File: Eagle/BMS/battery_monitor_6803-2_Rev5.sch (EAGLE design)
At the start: 68 parts, among them IC1 MIC2954-03WS, Q1 MOSFET-PCHANNELIRLML2244, Q10 IRF9530, Q2 MOSFET-NCHANNELBSS138, Q3 MOSFET-PCHANNELIRLML2244, Q4 MOSFET-PCHANNELIRLML2244, Q5 MOSFET-PCHANNELIRLML2244, Q6 MOSFET-NCHANNELBSS138, Q7 MOSFET-NCHANNELBSS138, Q8 MOSFET-NCHANNELBSS138, Q9 PMOS_AO4435

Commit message: Added voltage regulator to charging circuit of BMS.
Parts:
- removed A0: (no value), SparkFun:SOLDERJUMPER_2WAYS
- removed U$7: TACTILE-SWITCH-7914G, GeekAmmo:TACTILE-SWITCH-7914G
- removed U$8: ARDUINO_R3_SHIELD, SparkFun-Boards:ARDUINO_R3_SHIELD
- added A4: (no value), SparkFun:SOLDERJUMPER_2WAYS
- added D3: SMD26PL-TP, SparkFun-DiscreteSemi:DIODESOD123
- added X1: W237-07P, con-wago-508:W237-07P
- C1: value 0.1uF -> 1uF; MF AVX CORPORATION -> (none); MPN 0603YG104ZAT2A -> C0603X5R0J105M030BC; OC_NEWARK 01H6821 -> 04X3184; PROD_ID (none) -> CAP-08390; VALUE (none) -> 0.1uF
- C4: value 1uF -> 0.1uF; MF (none) -> AVX CORPORATION; MPN C0603X5R0J105M030BC -> 0603YG104ZAT2A; OC_NEWARK 04X3184 -> 01H6821; PROD_ID CAP-08390 -> (none); VALUE 0.1uF -> (none)
- R11: value 100k -> 4.7k; MF FARNELL -> VISHAY/DALE; MPN MC0063W06035100K -> CRCW06034K70FKEA; OC_NEWARK 39K0075 -> 52K8494
- R12: value 4.7k -> 100k; MF VISHAY/DALE -> FARNELL; MPN CRCW06034K70FKEA -> MC0063W06035100K; OC_NEWARK 52K8494 -> 39K0075
- R15: value 4.7k -> 470; MF VISHAY/DALE -> (none); MPN CRCW06034K70FKEA -> ERJ-P03F4700V; OC_NEWARK 52K8494 -> 05X8640; PROD_ID (none) -> RES-07851
- R17: value 470 -> 4.7k; MF (none) -> VISHAY/DALE; MPN ERJ-P03F4700V -> CRCW06034K70FKEA; OC_NEWARK 05X8640 -> 52K8494; PROD_ID RES-07851 -> (none)
- R18: value 470 -> 4.7k; MF (none) -> VISHAY/DALE; MPN ERJ-P03F4700V -> CRCW06034K70FKEA; OC_NEWARK 05X8640 -> 52K8494
- R20: value 4.7k -> 470; MF VISHAY/DALE -> (none); MPN CRCW06034K70FKEA -> ERJ-P03F4700V; OC_NEWARK 52K8494 -> 05X8640
- R21: value 4.7k -> 1Meg; MF VISHAY/DALE -> (none); MPN CRCW06034K70FKEA -> ERJ-3EKF1004V; OC_NEWARK 52K8494 -> 64R5311
- R24: value 1Meg -> 4.7k; MF (none) -> VISHAY/DALE; MPN ERJ-3EKF1004V -> CRCW06034K70FKEA; OC_NEWARK 64R5311 -> 52K8494
- R3: value 3.3k -> 100; MF VISHAY/DALE -> (none); MPN CRCW06033K00FKEA -> ERJ-1GNF1000C; OC_NEWARK 52K8368 -> 05X8794
- R4: value 100 -> 3.3k; MF (none) -> VISHAY/DALE; MPN ERJ-1GNF1000C -> CRCW06033K00FKEA; OC_NEWARK 05X8794 -> 52K8368
- U$3: value RESISTOR-POWER-3W -> TACTILE-SWITCH-7914G; device isaac1:RESISTOR-POWER-3W -> GeekAmmo:TACTILE-SWITCH-7914G; MF (none) -> BOURNS, INC.; MPN ERG-3SJ200 -> 7914G-1-000E; OC_NEWARK 52W7905 -> 05B2757
- U$4: value SCREW_TERMINAL_4 -> RESISTOR-POWER-3W; device isaac1:SCREW_TERMINAL_4 -> isaac1:RESISTOR-POWER-3W; MF TYCO ELECTRONICS -> (none); MPN 282834-4 -> ERG-3SJ200; OC_NEWARK 12H8388 -> 52W7905
- U$5: value LTC6803-2 -> ARDUINO_R3_SHIELD; device isaac1:LTC6803-2 -> SparkFun-Boards:ARDUINO_R3_SHIELD
- U$6: value SCREW_TERMINAL_2 -> LTC6803-2; device Isaac:SCREW_TERMINAL_2 -> isaac1:LTC6803-2; MF TYCO ELECTRONICS -> (none); MPN 282834-2 -> (none); OC_NEWARK 12H8386 -> unknown
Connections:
- removed net 5VREG: IC1.VO, Q10.S, R26.2
- removed net NONE: D2.C, U$4.P$4
- removed net VIN: D2.A, Q10.D, U$8.VIN
- new net 12VREG: D2.A, IC1.VO, U$5.VIN
- new net 12VUNREG: D3.A, IC1.VI, Q10.D
- new net N$26: D3.C, X1-5.KL
- new net WIRE: D2.C, X1-4.KL
- net +5: now also R13.2, R17.2, R21.1, R24.2, U$5.5V; no longer R14.2, R15.2, R21.2, R24.1, U$8.5V
- net ALL_SYSTEMS_GO: now also Q2.G, R11.2, U$5.D8; no longer Q6.G, R13.2, U$8.D8
- net BATTERY+: now also Q10.S, R26.2, X1-1.KL; no longer IC1.VI, U$4.P$1
- net CHARGE: now also R14.2, U$5.*D9; no longer R12.2, U$8.*D9
- net CHARGER_CONNECTED: now also R19.2, U$5.D7; no longer R20.2, U$8.D7
- net CHARGER_IN: now also R18.2, X1-3.KL; no longer R19.2, U$4.P$3
- net ESTOP1: now also U$3.3, U$3.4, X1-6.KL; no longer U$6.P$1, U$7.3, U$7.4
- net ESTOP2: now also Q2.D, X1-7.KL; no longer Q6.D, U$6.P$2
- net GND: now also A4.3, C1.1, C7.2, DZ3.A, R11.1, R14.1, R18.1, U$3.1, U$3.2, U$5.GND@0, U$5.GND@1, U$5.GND@2, U$6.V-, X1-2.KL; no longer A0.3, C1.2, C7.1, DZ1.A, R12.1, R13.1, R20.1, U$4.P$2, U$5.V-, U$7.1, U$7.2, U$8.GND@0, U$8.GND@1, U$8.GND@2
- net MISO: now also R24.1, U$5.D12, U$6.SDO; no longer R21.1, U$5.SDO, U$8.D12
- net MOSI: now also U$5.*D11, U$6.SDI; no longer U$5.SDI, U$8.*D11
- net N$10: now also Q3.D, R16.2; no longer Q4.D, R17.2
- net N$11: now also Q3.G; no longer Q4.G
- net N$12: now also R20.2, U$4.P$1; no longer R18.2, U$3.P$1
- net N$13: now also R15.1; no longer R16.1
- net N$14: now also C2.1, DZ1.C, R7.2, U$6.C3; no longer C1.1, DZ3.C, R6.2, U$5.C3
- net N$15: now also C4.1, DZ3.C, R6.2, U$6.C1; no longer C3.1, DZ1.C, R4.2, U$5.C1
- net N$16: now also C3.1, DZ1.A, R3.2, U$6.C2; no longer C2.1, DZ3.A, R5.2, U$5.C2
- net N$17: now also R5.2, U$6.C10, U$6.C11, U$6.C12, U$6.C4, U$6.C5, U$6.C6, U$6.C7, U$6.C8, U$6.C9; no longer R7.2, U$5.C10, U$5.C11, U$5.C12, U$5.C4, U$5.C5, U$5.C6, U$5.C7, U$5.C8, U$5.C9
- net N$18: now also Q4.D; no longer Q1.D
- net N$19: now also C1.2, Q4.S, U$6.V+; no longer C5.2, Q1.S, U$5.V+
- net N$2: now also Q1.S, R6.1; no longer Q3.S, R4.1
- net N$20: now also Q4.G, Q6.D; no longer Q1.G, Q2.D
- net N$21: now also C6.2, R12.1, U$6.VTEMP1; no longer C7.2, R11.1, U$5.VTEMP1
- net N$22: now also R16.1; no longer R17.1
- net N$23: now also R20.1; no longer R18.1
- net N$24: now also R21.2, U$6.GPIO2; no longer R22.2, U$5.GPIO2
- net N$25: now also U$6.GPIO1; no longer U$5.GPIO1
- net N$27: now also R22.2, U$6.WDTB; no longer R24.2, U$5.WDTB
- net N$28: now also A2.2, U$6.A3; no longer A3.2, U$5.A3
- net N$29: now also R4.1; no longer R3.1
- net N$3: now also Q3.S, R3.1, U$4.P$2; no longer Q4.S, R5.1, U$3.P$2
- net N$30: now also A4.2, U$6.A2; no longer A2.2, U$5.A2
- net N$31: now also U$6.A1; no longer U$5.A1
- net N$32: now also A3.2, U$6.AO; no longer A0.2, U$5.AO
- net N$33: now also U$6.TOS; no longer U$5.TOS
- net N$34: now also C5.2, U$6.VREF; no longer C6.2, U$5.VREF
- net N$4: now also R5.1; no longer R6.1
- net N$5: now also Q1.D, R15.2; no longer Q3.D, R16.2
- net N$6: now also U$6.S2; no longer U$5.S2
- net N$7: now also Q1.G; no longer Q3.G
- net N$8: now also U$6.S1; no longer U$5.S1
- net N$9: now also R4.2, U$6.S3; no longer R3.2, U$5.S3
- net PWR: now also Q6.G, U$5.*D6; no longer Q2.G, U$8.*D6
- net SCK: now also U$5.D13, U$6.SCKI; no longer U$5.SCKI, U$8.D13
- net SCL: now also R17.1, U$5.SCL; no longer R15.1, U$8.SCL
- net SDA: now also R13.1, U$5.SDA; no longer R14.1, U$8.SDA
- net SS: now also U$5.*D10, U$6.CSBI; no longer U$5.CSBI, U$8.*D10
- net VREG: now also A4.1, C7.1, R12.2, U$6.VREG; no longer A0.1, C4.1, R11.2, U$5.VREG
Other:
- moved on the sheet: A2, A3, C1, C2, C3, C4, C5, C6, C7, D2, DZ1, DZ3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

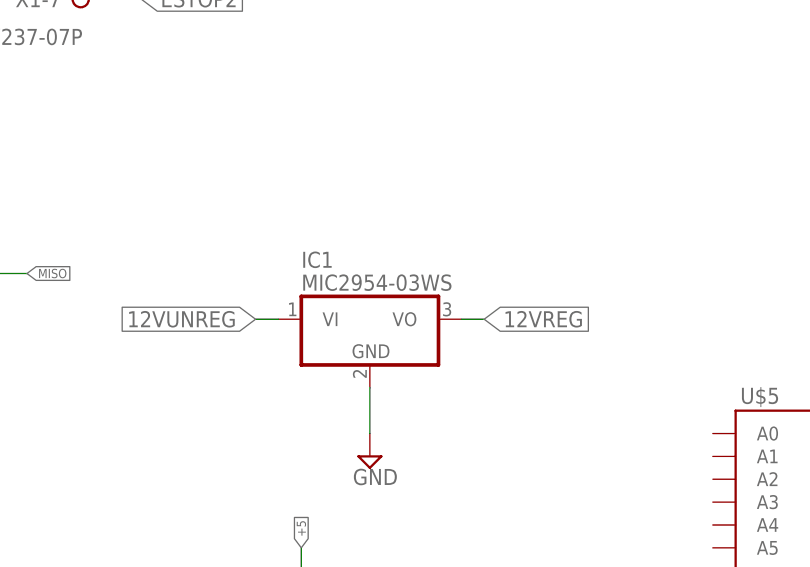
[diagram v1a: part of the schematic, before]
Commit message: Changed linear regulator device.
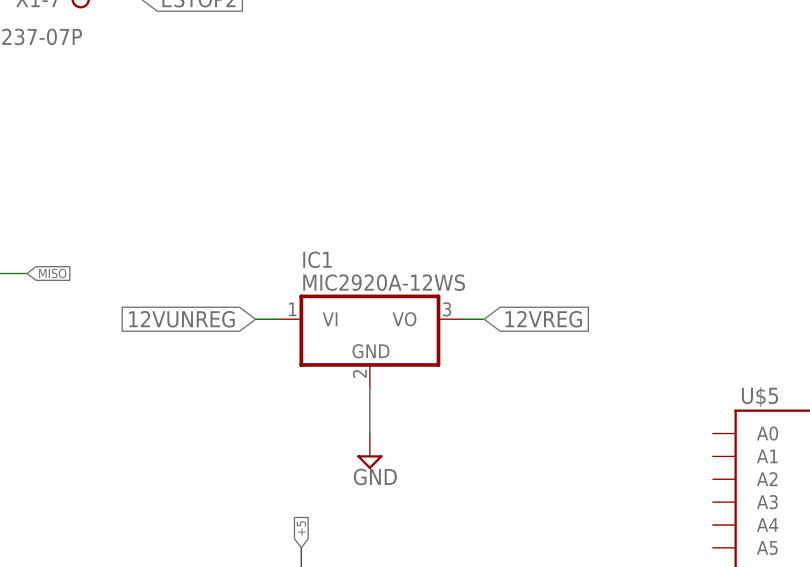
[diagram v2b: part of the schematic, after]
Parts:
- IC1: value MIC2954-03WS -> MIC2920A-12WS
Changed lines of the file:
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@@
 <part name="SUPPLY19" library="supply2" deviceset="GND" device=""/>
 <part name="D1" library="SparkFun-DiscreteSemi" deviceset="DIODE" device="SOD123" value="SMD26PL-TP"/>
-<part name="IC1" library="linear" deviceset="MCP1703" device="DB" value="MIC2954-03WS"/>
+<part name="IC1" library="linear" deviceset="MCP1703" device="DB" value="MIC2920A-12WS"/>
 <part name="SUPPLY20" library="supply2" deviceset="GND" device=""/>
 <part name="D3" library="SparkFun-DiscreteSemi" deviceset="DIODE" device="SOD123" value="SMD26PL-TP"/>
